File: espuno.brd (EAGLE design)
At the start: 68.6 x 53.3 mm, 61 parts, among them IC1 REG1117, J1 ARDUINO_R3_SHIELD, T1 FDN340P, U1 ADS1115IDGST, U2 NCP1117ST50T3G, U4 FT232R, U5 LMV358IDGKR, U6 MCP73831, U7 TPS61200, X1 POWERSUPPLY_DC21MMX

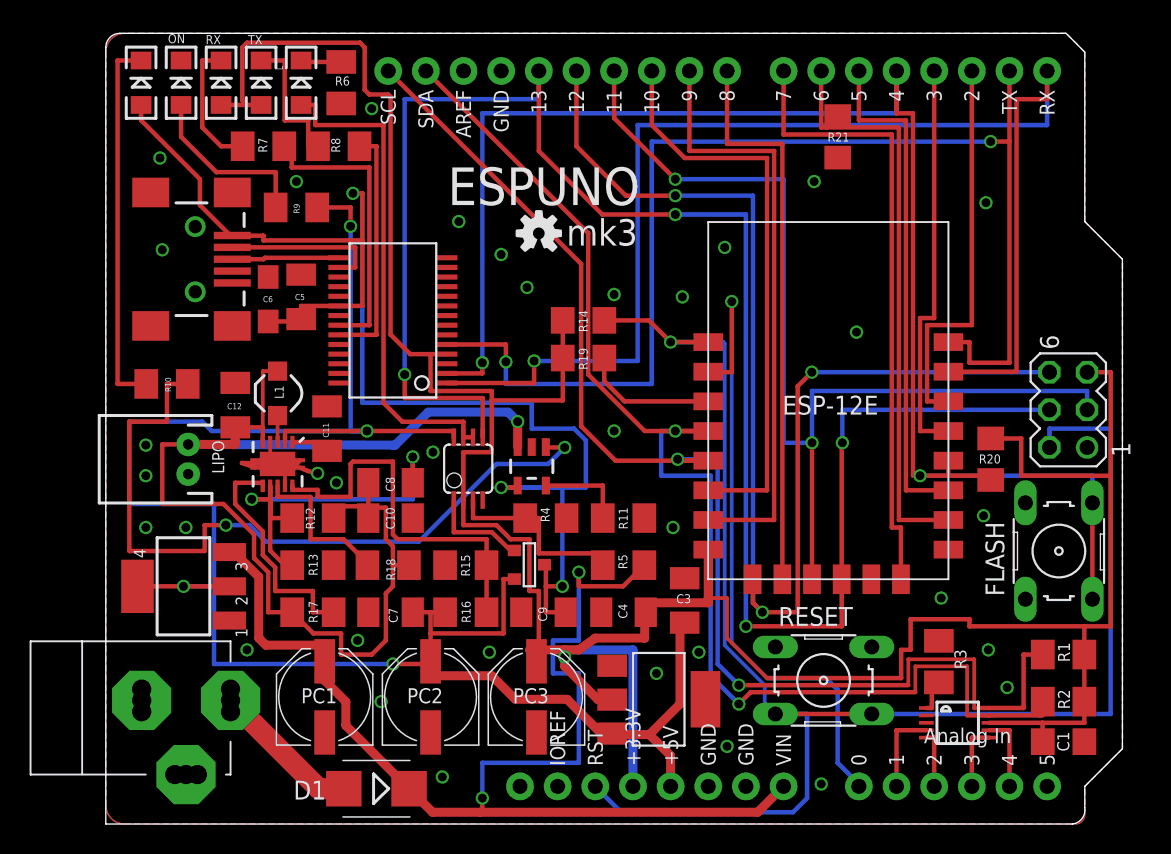
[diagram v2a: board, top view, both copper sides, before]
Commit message: Use two ADS1015's and a CAT9531 to interface with the outside world.
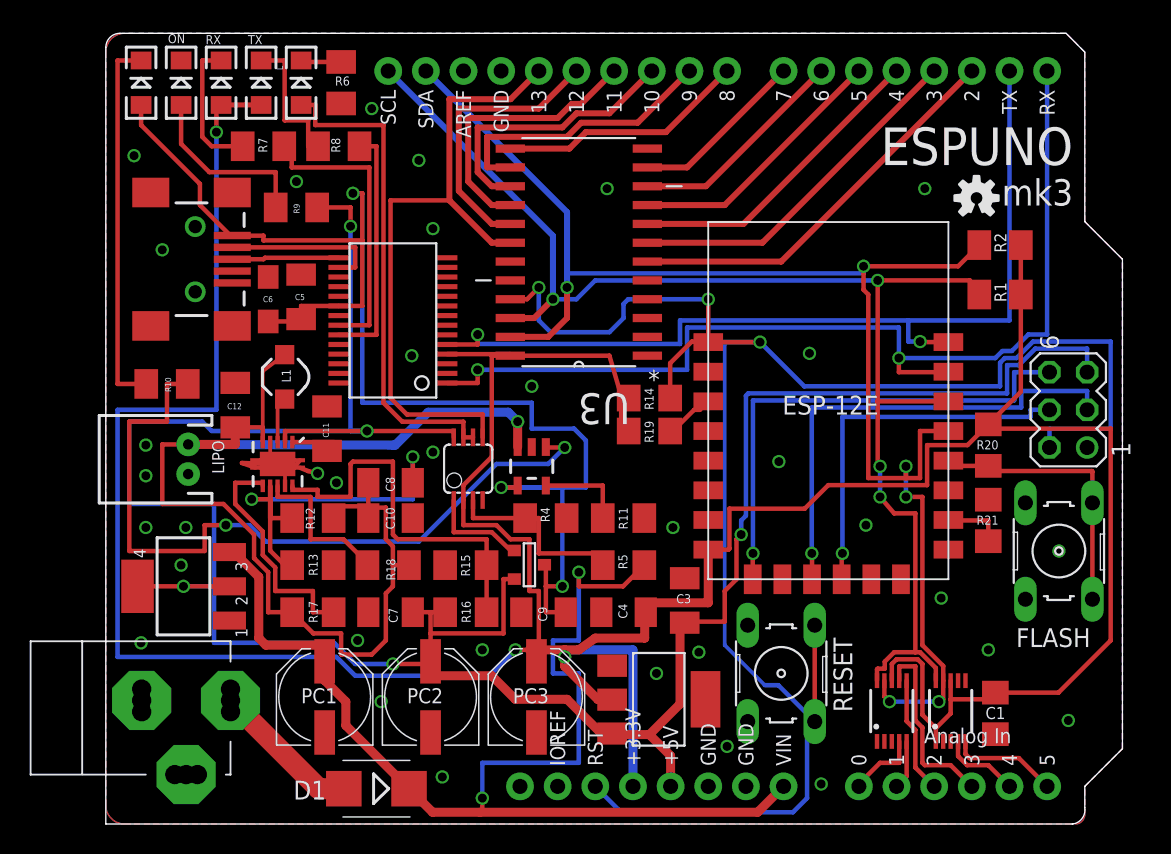
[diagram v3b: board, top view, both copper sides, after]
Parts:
- removed R3: 10K, rcl:M1206
- added U3: CAT9532WI, ON Semiconductor_By_element14_Batch_1:SOIC127P1031X265-24N
- added U8: ADS1015, SparkFun-AnalogIC:MSOP10
- U1: value ADS1115IDGST -> ADS1015; device microbuilder:MSOP10 -> SparkFun-AnalogIC:MSOP10
- moved R2 31.1 mm to (60.3, 39.1)
- moved LOGO1 29.6 mm to (58.7, 42.2)
- moved R21 27.8 mm to (59.5, 20.5), turned to 270 degrees
- moved R1 24.7 mm to (60.3, 35.7)
- moved R14 6.87 mm to (36.7, 28.7)
- moved R19 6.63 mm to (36.7, 26.5)
- moved C1 4.98 mm to (60.0, 7.46), turned to 90 degrees
- moved RESET 2.90 mm to (45.6, 10.2), turned to 90 degrees
- moved L1 1.21 mm to (12.1, 30.2)
- moved R20 0.97 mm to (59.5, 25.6)
- moved U1 0.93 mm to (57.0, 7.62), turned to 0 degrees
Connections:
- net N$28 renamed CS0
- removed net 10/GPIO12: J1.D10, MDL1.6
- removed net 11/MOSI: J1.D11, MDL1.21, SV1.3
- removed net 12/MISO: J1.D12, MDL1.18, SV1.6
- removed net 13/SCLK: J1.D13, MDL1.22, SV1.4, U5.5
- removed net 2/GPIO5: J1.D2, MDL1.14
- removed net 3/GPIO4: J1.D3, MDL1.13
- removed net 4/GPIO0: FLASH.3, FLASH.4, J1.D4, MDL1.12, R20.2, U4.2
- removed net 5/GPIO2: J1.D5, MDL1.11
- removed net 6/GPIO15: J1.D6, MDL1.10, R21.2
- removed net 7/GPIO10: J1.D7, MDL1.20
- removed net 8/GPIO9: J1.D8, MDL1.19
- removed net 9/GPIO13: J1.D9, MDL1.7
- removed net ADDR: R3.1, U1.1
- removed net SCL/GPIO14: J1.SCL, MDL1.5, R1.2, U1.10
- removed net SDA/GPIO16: J1.SDA, MDL1.4, R2.2, U1.9
- new net AIN5: J1.A5, U1.5
- new net D0: U3.4
- new net D1: U3.5
- new net D10: J1.D10, U3.15
- new net D11: J1.D11, U3.16
- new net D12: J1.D12, U3.17
- new net D13: J1.D13, U3.18, U5.5
- new net D14: U3.19
- new net D15: U3.20
- new net D2: J1.D2, U3.6
- new net D3: J1.D3, U3.7
- new net D4: J1.D4, U3.8
- new net D5: J1.D5, U3.9
- new net D6: J1.D6, U3.10
- new net D7: J1.D7, U3.11
- new net D8: J1.D8, U3.13
- new net D9: J1.D9, U3.14
- new net GPIO0: FLASH.3, FLASH.4, MDL1.12, R20.2
- new net GPIO10: MDL1.20
- new net GPIO12: MDL1.6
- new net GPIO13: MDL1.7
- new net GPIO14: MDL1.5
- new net GPIO15: MDL1.10, R21.2
- new net GPIO16: MDL1.4
- new net GPIO2: MDL1.11
- new net GPIO9: MDL1.19
- new net MISO: MDL1.18, SV1.6
- new net MOSI: MDL1.21, SV1.3
- new net SCL: J1.SCL, MDL1.14, R1.2, U1.10, U3.22, U8.10
- new net SCLK: MDL1.22, SV1.4
- new net SDA: J1.SDA, MDL1.13, R2.2, U1.9, U3.23, U8.9
- net 3.3V: now also U1.1, U3.24, U8.8; no longer SV1.5
- net 5V: now also SV1.5
- net ADC: no longer J1.A0
- net AIN0: now also J1.A0, U8.4; no longer J1.A1, U1.4
- net AIN1: now also J1.A1, U8.5; no longer J1.A2, U1.5
- net AIN2: now also J1.A2, U8.6; no longer J1.A3, U1.6
- net AIN3: now also J1.A3, U8.7; no longer J1.A4, U1.7
- net AIN4: now also J1.A4, U1.4; no longer J1.A5
- net GND: now also U3.1, U3.12, U3.2, U3.3, U8.1, U8.3; no longer R3.2
- net RESET: now also U3.21
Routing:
- net 13/SCLK: track 123.0 -> 0.00 mm, vias 4 -> 0
- net 4/GPIO0: track 105.6 -> 0.00 mm, vias 2 -> 0
- net SDA: track 0.00 -> 100.3 mm, vias 0 -> 6
- net SCL: track 0.00 -> 91.8 mm, vias 0 -> 4
- net SCL/GPIO14: track 88.7 -> 0.00 mm, vias 2 -> 0
- net SDA/GPIO16: track 87.4 -> 0.00 mm, vias 2 -> 0
- net 12/MISO: track 84.2 -> 0.00 mm, vias 3 -> 0
- net 11/MOSI: track 68.5 -> 0.00 mm, vias 2 -> 0
- net 3.3V: track 202.3 -> 252.0 mm, vias 1 -> 3
- net ADC: track 44.9 -> 0.00 mm, vias 1 -> 0
- net 5V: track 137.4 -> 182.2 mm, vias 4 -> 5
- net D13: track 0.00 -> 44.5 mm
- net 7/GPIO10: track 42.2 -> 0.00 mm
- net 9/GPIO13: track 40.4 -> 0.00 mm
- net 6/GPIO15: track 40.0 -> 0.00 mm
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
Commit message: move adc bits up a bit away from the port
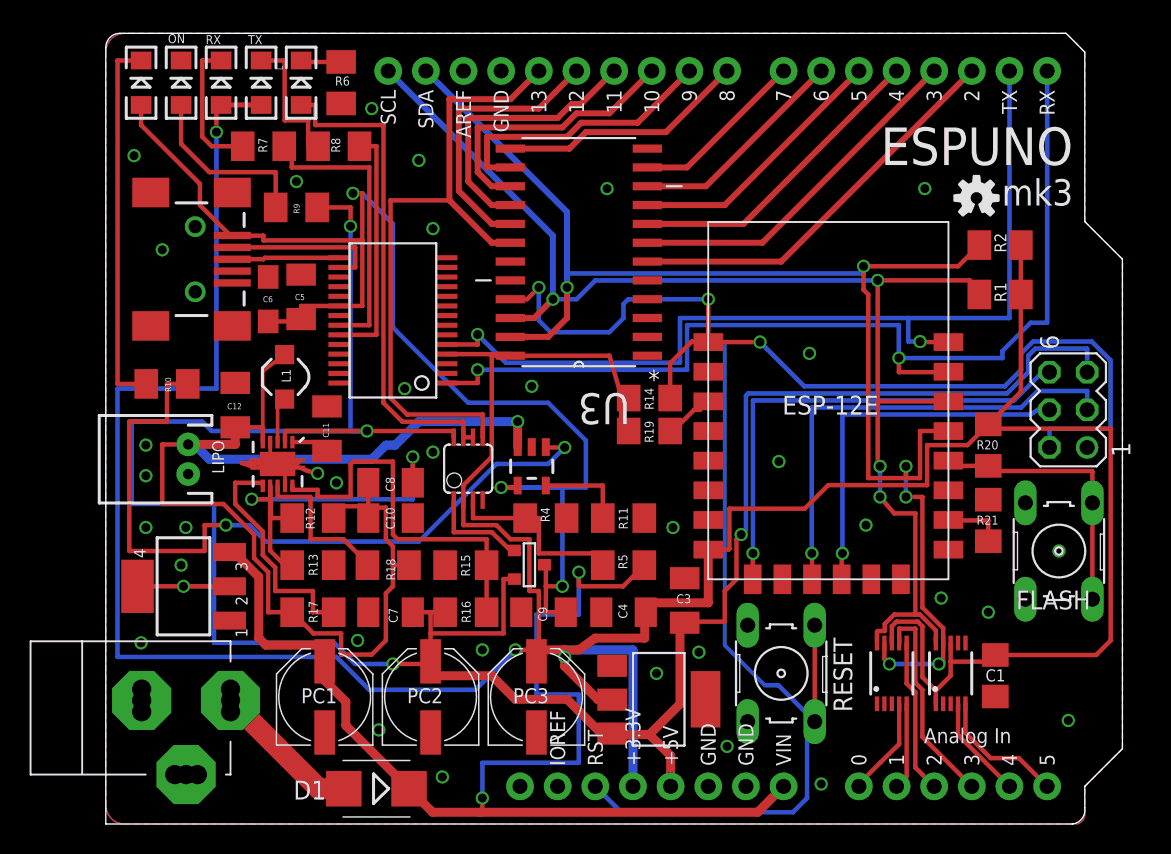
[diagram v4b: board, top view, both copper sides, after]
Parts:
- moved C1 2.54 mm to (60.0, 10.0)
- moved U1 2.54 mm to (57.0, 10.2)
- moved U8 2.54 mm to (53.0, 10.2)
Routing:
- net USBVCC: track 94.8 -> 89.5 mm
- net AIN2: track 7.90 -> 10.4 mm
- net AIN1: track 3.31 -> 5.85 mm
- net SDA: track 100.3 -> 97.8 mm
- net SCL: track 91.8 -> 89.2 mm
- net VIN: track 82.4 -> 84.7 mm
- net AIN0: track 4.92 -> 6.70 mm
- net AIN5: track 7.26 -> 8.97 mm
- net AIN4: track 5.30 -> 7.01 mm
- net TX: track 61.8 -> 63.4 mm
- net AIN3: track 12.8 -> 14.3 mm
- net RESET: track 127.7 -> 126.5 mm
- net MISO: track 34.0 -> 32.9 mm
- net 5V: track 182.2 -> 181.4 mm
- net MOSI: track 32.6 -> 31.9 mm

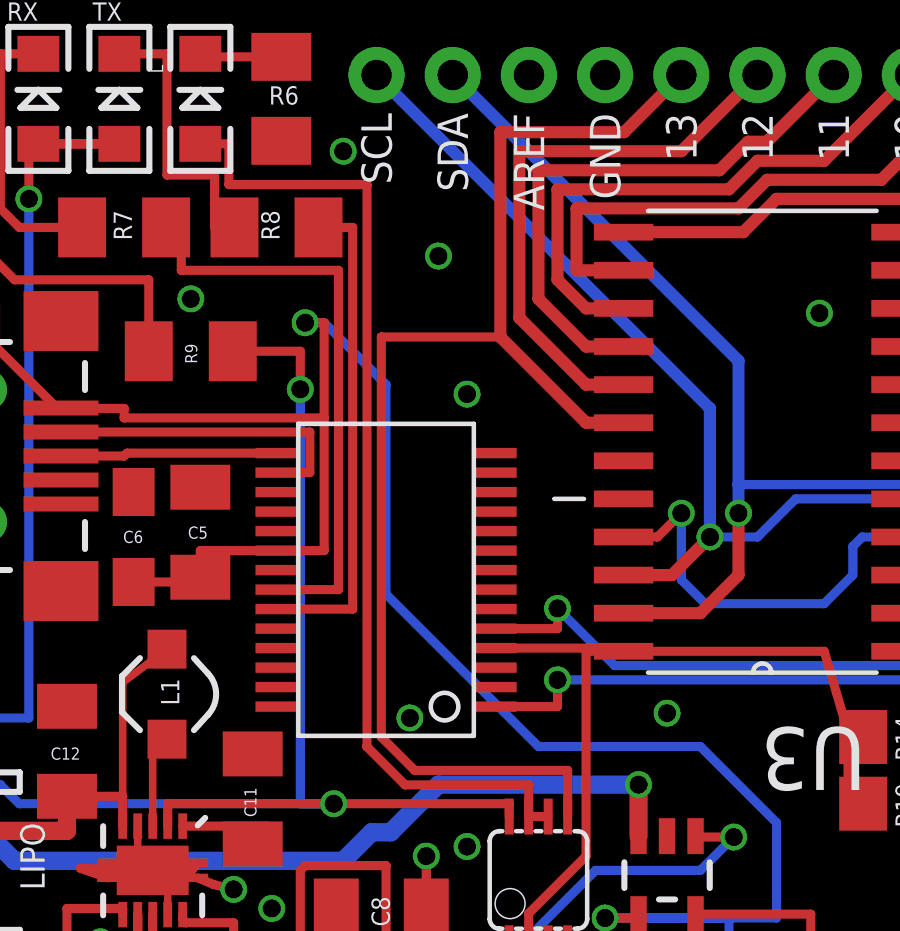
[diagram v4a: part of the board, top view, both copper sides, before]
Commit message: Make the FT232R consume its own 3.3v so I can test it by merely attaching USB.
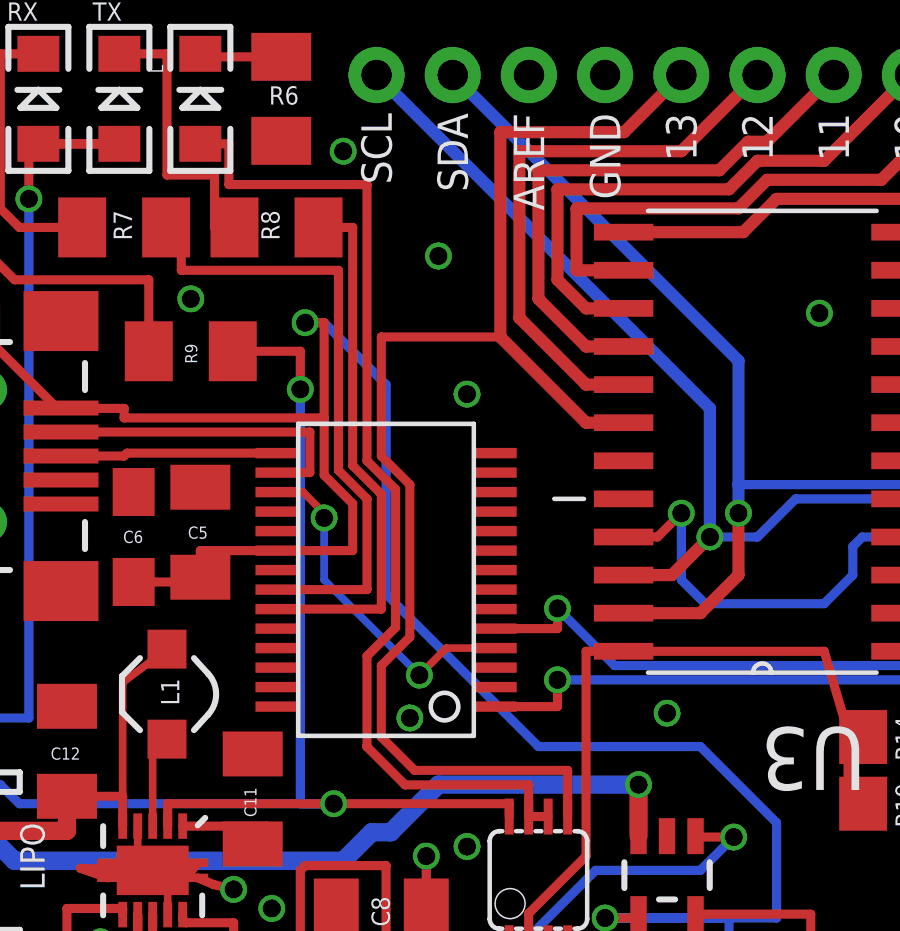
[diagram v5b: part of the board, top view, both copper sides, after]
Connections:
- new net N$10: U4.17, U4.4
- net 3.3V: no longer U4.4
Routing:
- net N$10: track 0.00 -> 11.5 mm, vias 0 -> 2
- net 3.3V: track 251.7 -> 247.5 mm
- net USBVCC: track 89.5 -> 90.9 mm
- net N$7: track 19.9 -> 21.2 mm
- net N$9: track 16.6 -> 17.9 mm
- net L13: track 33.3 -> 34.1 mm
- net D13: track 44.5 -> 45.2 mm
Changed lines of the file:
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@@
 <contactref element="C4" pad="2"/>
 <contactref element="U5" pad="2"/>
-<contactref element="U4" pad="4"/>
 <contactref element="RX" pad="A"/>
 <contactref element="TX" pad="A"/>
@@
 <wire x1="30.95625" y1="10.63625" x2="30.95625" y2="11.27125" width="0.6096" layer="1"/>
 <contactref element="U3" pad="24"/>
-<wire x1="23.0235" y1="31.6975" x2="27.28595" y2="31.6975" width="0.3048" layer="1"/>
 <wire x1="27.28595" y1="31.6975" x2="27.28595" y2="31.59125" width="0.3048" layer="1"/>
 <wire x1="24.1215" y1="21.85825" x2="24.1215" y2="22.8515" width="0.3048" layer="1"/>
@@
 <contactref element="D4" pad="A"/>
 <contactref element="JP1" pad="VBUS"/>
-<wire x1="15.7115" y1="34.9475" x2="17.30375" y2="34.9475" width="0.3048" layer="1"/>
-<wire x1="17.30375" y1="34.9475" x2="17.30375" y2="39.37" width="0.3048" layer="1"/>
+<wire x1="15.7115" y1="34.9475" x2="18.25625" y2="34.9475" width="0.3048" layer="1"/>
+<wire x1="18.25625" y1="34.9475" x2="18.25625" y2="36.5125" width="0.3048" layer="1"/>
+<wire x1="18.25625" y1="36.5125" x2="17.30375" y2="37.465" width="0.3048" layer="1"/>
+<wire x1="17.30375" y1="37.465" x2="17.30375" y2="39.37" width="0.3048" layer="1"/>
 <wire x1="17.30375" y1="39.37" x2="10.63625" y2="39.37" width="0.3048" layer="1"/>
 <wire x1="10.63625" y1="39.37" x2="10.63625" y2="39.6875" width="0.3048" layer="1"/>
@@
 <wire x1="14.12875" y1="48.50625" x2="14.12875" y2="47.14875" width="0.3048" layer="1"/>
 <wire x1="14.12875" y1="47.14875" x2="18.7325" y2="47.14875" width="0.3048" layer="1"/>
-<wire x1="18.7325" y1="47.14875" x2="18.7325" y2="28.41625" width="0.3048" layer="1"/>
+<wire x1="18.7325" y1="47.14875" x2="18.7325" y2="37.94125" width="0.3048" layer="1"/>
+<wire x1="18.7325" y1="37.94125" x2="19.685" y2="36.98875" width="0.3048" layer="1"/>
+<wire x1="19.685" y1="36.98875" x2="19.685" y2="32.385" width="0.3048" layer="1"/>
+<wire x1="19.685" y1="32.385" x2="18.7325" y2="31.4325" width="0.3048" layer="1"/>
+<wire x1="18.7325" y1="31.4325" x2="18.7325" y2="28.41625" width="0.3048" layer="1"/>
 <wire x1="18.7325" y1="28.41625" x2="18.724" y2="28.41625" width="0.3048" layer="1"/>
 <wire x1="24.7715" y1="26.08325" x2="24.1215" y2="26.08325" width="0.3048" layer="1"/>
@@
 <wire x1="12.54125" y1="45.56125" x2="12.54125" y2="44.29125" width="0.3048" layer="1"/>
 <wire x1="12.54125" y1="44.29125" x2="17.78" y2="44.29125" width="0.3048" layer="1"/>
-<wire x1="17.78" y1="44.29125" x2="17.78" y2="33.6475" width="0.3048" layer="1"/>
-<wire x1="17.78" y1="33.6475" x2="15.7115" y2="33.6475" width="0.3048" layer="1"/>
+<wire x1="17.78" y1="44.29125" x2="17.78" y2="37.62375" width="0.3048" layer="1"/>
+<wire x1="17.78" y1="37.62375" x2="18.7325" y2="36.67125" width="0.3048" layer="1"/>
+<wire x1="18.7325" y1="36.67125" x2="18.7325" y2="33.6475" width="0.3048" layer="1"/>
+<wire x1="18.7325" y1="33.6475" x2="15.7115" y2="33.6475" width="0.3048" layer="1"/>
 </signal>
 <signal name="N$9">
@@
 <wire x1="17.11625" y1="45.72" x2="16.9575" y2="45.72" width="0.3048" layer="1"/>
 <wire x1="17.11625" y1="45.72" x2="18.25625" y2="45.72" width="0.3048" layer="1"/>
-<wire x1="18.25625" y1="45.72" x2="18.25625" y2="32.9975" width="0.3048" layer="1"/>
-<wire x1="18.25625" y1="32.9975" x2="15.7115" y2="32.9975" width="0.3048" layer="1"/>
+<wire x1="18.25625" y1="45.72" x2="18.25625" y2="37.7825" width="0.3048" layer="1"/>
+<wire x1="18.25625" y1="37.7825" x2="19.20875" y2="36.83" width="0.3048" layer="1"/>
+<wire x1="19.20875" y1="36.83" x2="19.20875" y2="32.9975" width="0.3048" layer="1"/>
+<wire x1="19.20875" y1="32.9975" x2="15.7115" y2="32.9975" width="0.3048" layer="1"/>
 </signal>
 <signal name="SCL">
@@
 <wire x1="25.4215" y1="27.6225" x2="20.32" y2="27.6225" width="0.3048" layer="1"/>
 <wire x1="20.32" y1="27.6225" x2="19.20875" y2="28.73375" width="0.3048" layer="1"/>
-<wire x1="19.20875" y1="28.73375" x2="19.20875" y2="42.06875" width="0.3048" layer="1"/>
+<wire x1="19.20875" y1="28.73375" x2="19.20875" y2="31.115" width="0.3048" layer="1"/>
+<wire x1="19.20875" y1="31.115" x2="20.16125" y2="32.0675" width="0.3048" layer="1"/>
+<wire x1="20.16125" y1="32.0675" x2="20.16125" y2="37.1475" width="0.3048" layer="1"/>
+<wire x1="20.16125" y1="37.1475" x2="19.20875" y2="38.1" width="0.3048" layer="1"/>
+<wire x1="19.20875" y1="38.1" x2="19.20875" y2="42.06875" width="0.3048" layer="1"/>
 <wire x1="19.20875" y1="42.06875" x2="23.1775" y2="42.06875" width="0.3048" layer="1"/>
 </signal>
@@
 <wire x1="57.49125" y1="6.00875" x2="60.96" y2="2.54" width="0.3048" layer="1"/>
 </signal>
+<signal name="N$10">
+<contactref element="U4" pad="4"/>
+<contactref element="U4" pad="17"/>
+<wire x1="15.7115" y1="36.8975" x2="16.60125" y2="36.8975" width="0.254" layer="1"/>
+<wire x1="16.60125" y1="36.8975" x2="17.30375" y2="36.195" width="0.254" layer="1"/>
+<wire x1="17.30375" y1="36.195" x2="17.30375" y2="36.03625" width="0.254" layer="1"/>
+<via x="17.30375" y="36.03625" extent="1-16" drill="0.6"/>
+<wire x1="17.30375" y1="36.03625" x2="17.30375" y2="33.9725" width="0.254" layer="16"/>
+<wire x1="17.30375" y1="33.9725" x2="20.47875" y2="30.7975" width="0.254" layer="16"/>
+<via x="20.47875" y="30.7975" extent="1-16" drill="0.6"/>
+<wire x1="20.47875" y1="30.7975" x2="21.37875" y2="31.6975" width="0.254" layer="1"/>
+<wire x1="21.37875" y1="31.6975" x2="23.0235" y2="31.6975" width="0.254" layer="1"/>
+</signal>
 </signals>
